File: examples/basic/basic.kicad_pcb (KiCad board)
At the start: 2 copper layers, 9 x 14 mm, 7 parts

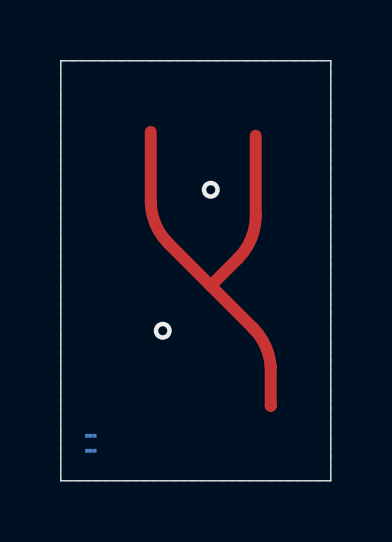
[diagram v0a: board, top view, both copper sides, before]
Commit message: Proof of concept mods for modeling a resistor
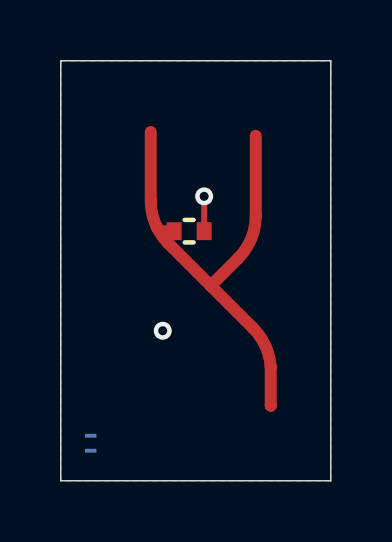
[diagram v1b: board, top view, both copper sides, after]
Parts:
- added R1: 10r 0402 0.1% thinfilm, 1self_passives:R_0402_1005Metric, F.Cu at (144.3, 106.7)
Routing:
- net GND: track 0.00 -> 1.16 mm
- net /MSL: track 16.1 -> 17.2 mm
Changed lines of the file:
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@@
     (property "Sheetfile" "basic.kicad_sch")
     (property "Sheetname" "")
+    (property "ki_description" "Net tie, 2 pins")
+    (property "ki_keywords" "net tie short")
     (attr through_hole exclude_from_pos_files)
     (net_tie_pad_groups "1, 2")
@@
     (at 146.5 103.25 180)
     (descr "Place where port in the simulation should be located. Set it's reference to SPx, where x is port number")
-    (attr board_only exclude_from_pos_files exclude_from_bom)
+    (attr board_only exclude_from_bom)
     (fp_text reference "SP3" (at 0 1 180 unlocked) (layer "F.Fab")
         (effects (font (size 1 1) (thickness 0.15)))
@@
     (at 147 112.75)
     (descr "Place where port in the simulation should be located. Set it's reference to SPx, where x is port number")
-    (attr board_only exclude_from_pos_files exclude_from_bom)
+    (attr board_only exclude_from_bom)
     (fp_text reference "SP2" (at 0 1 unlocked) (layer "F.Fab")
         (effects (font (size 1 1) (thickness 0.15)))
@@
     (property "Sheetfile" "basic.kicad_sch")
     (property "Sheetname" "")
+    (property "ki_description" "Net tie, 2 pins")
+    (property "ki_keywords" "net tie short")
     (attr through_hole exclude_from_pos_files)
     (net_tie_pad_groups "1, 2")
@@
       (net 1 "/MSL") (pinfunction "2") (pintype "passive"))
   )
+  (footprint "1self_passives:R_0402_1005Metric" (layer "F.Cu")
+    (at 144.28 106.68)
+    (descr "Resistor SMD 0402 (1005 Metric), square (rectangular) end terminal, IPC_7351 nominal, (Body size source: http://www.tortai-tech.com/upload/download/2011102023233369053.pdf), generated with kicad-footprint-generator")
+    (tags "resistor")
+    (property "AVR" "TE Connectivity Passive Product")
+    (property "Description" "RES SMD 10 OHM 0.1% 1/16W 0402 ")
+    (property "Detailed Description" "10 Ohms ±0.1% 0.063W, 1/16W Chip Resistor 0402 (1005 Metric)  Thin Film")
+    (property "Mfg Part #" "CPF0402B10RE1")
+    (property "Sheetfile" "basic.kicad_sch")
+    (property "Sheetname" "")
+    (property "similar_resistors" " ")
+    (property "size(LWT,mm)" "1x0.5x0.35")
+    (attr smd)
+    (fp_text reference "R1" (at 0 -1.17) (layer "F.SilkS") hide
+        (effects (font (size 1 1) (thickness 0.15)))
+    )
+    (fp_text value "10r 0402 0.1% thinfilm" (at 0 1.17) (layer "F.Fab") hide
+        (effects (font (size 1 1) (thickness 0.15)))
+    )
+    (fp_text user "${REFERENCE}" (at 0 0) (layer "F.Fab")
+        (effects (font (size 0.25 0.25) (thickness 0.04)))
+    )
+    (fp_line (start -0.15 -0.375) (end 0.15 -0.375)
+      (stroke (width 0.15) (type solid)) (layer "F.SilkS"))
+    (fp_line (start -0.15 0.375) (end 0.15 0.375)
+      (stroke (width 0.15) (type solid)) (layer "F.SilkS"))
+    (fp_line (start -0.7 -0.25) (end -0.7 0.25)
+      (stroke (width 0.05) (type solid)) (layer "F.CrtYd"))
+    (fp_line (start -0.5 0.45) (end 0.5 0.45)
+      (stroke (width 0.05) (type solid)) (layer "F.CrtYd"))
+    (fp_line (start 0.5 -0.45) (end -0.5 -0.45)
+      (stroke (width 0.05) (type solid)) (layer "F.CrtYd"))
+    (fp_line (start 0.7 0.25) (end 0.7 -0.25)
+      (stroke (width 0.05) (type solid)) (layer "F.CrtYd"))
+    (fp_arc (start -0.7 -0.25) (mid -0.641421 -0.391421) (end -0.5 -0.45)
+      (stroke (width 0.05) (type solid)) (layer "F.CrtYd"))
+    (fp_arc (start -0.50187 0.45) (mid -0.643291 0.391421) (end -0.70187 0.25)
+      (stroke (width 0.05) (type solid)) (layer "F.CrtYd"))
+    (fp_arc (start 0.5 -0.45) (mid 0.641421 -0.391421) (end 0.7 -0.25)
+      (stroke (width 0.05) (type solid)) (layer "F.CrtYd"))
+    (fp_arc (start 0.7 0.25) (mid 0.641421 0.391421) (end 0.5 0.45)
+      (stroke (width 0.05) (type solid)) (layer "F.CrtYd"))
+    (fp_line (start -0.5 -0.25) (end 0.5 -0.25)
+      (stroke (width 0.1) (type solid)) (layer "F.Fab"))
+    (fp_line (start -0.5 0.25) (end -0.5 -0.25)
+      (stroke (width 0.1) (type solid)) (layer "F.Fab"))
+    (fp_line (start 0.5 -0.25) (end 0.5 0.25)
+      (stroke (width 0.1) (type solid)) (layer "F.Fab"))
+    (fp_line (start 0.5 0.25) (end -0.5 0.25)
+      (stroke (width 0.1) (type solid)) (layer "F.Fab"))
+    (pad "1" smd rect (at -0.5 0) (size 0.5 0.6) (layers "F.Cu" "F.Paste" "F.Mask")
+      (net 1 "/MSL") (pintype "passive"))
+    (pad "2" smd rect (at 0.5 0) (size 0.5 0.6) (layers "F.Cu" "F.Paste" "F.Mask")
+      (net 2 "GND") (pintype "passive"))
+    (model "${KICAD6_3DMODEL_DIR}/Resistor_SMD.3dshapes/R_0402_1005Metric.wrl"
+      (offset (xyz 0 0 0))
+      (scale (xyz 1 1 1))
+      (rotate (xyz 0 0 0))
+    )
+  )
   (footprint "antmicro-footprints:Simulation_Port" (layer "F.Cu")
     (at 143 103.25 180)
     (descr "Place where port in the simulation should be located. Set it's reference to SPx, where x is port number")
-    (attr board_only exclude_from_pos_files exclude_from_bom)
+    (attr board_only exclude_from_bom)
     (fp_text reference "SP1" (at 0 1 180 unlocked) (layer "F.Fab")
         (effects (font (size 1 1) (thickness 0.15)))
@@
     (property "Sheetfile" "basic.kicad_sch")
     (property "Sheetname" "")
+    (property "ki_description" "Net tie, 2 pins")
+    (property "ki_keywords" "net tie short")
     (attr through_hole exclude_from_pos_files)
     (net_tie_pad_groups "1, 2")
@@
     (property "Sheetfile" "basic.kicad_sch")
     (property "Sheetname" "")
+    (property "ki_description" "Net tie, 2 pins")
+    (property "ki_keywords" "net tie short")
     (attr through_hole exclude_from_pos_files)
     (net_tie_pad_groups "1, 2")
@@
   (segment (start 145 108.5) (end 145.914214 107.585786) (width 0.4) (layer "F.Cu") (net 1))
   (segment (start 146.998156 111.19746) (end 146.998156 112.498156) (width 0.4) (layer "F.Cu") (net 1))
+  (segment (start 143.773792 106.686208) (end 143.78 106.68) (width 0.4) (layer "F.Cu") (net 1))
   (segment (start 146.5 106.171573) (end 146.5 103.5) (width 0.4) (layer "F.Cu") (net 1))
+  (segment (start 143.585787 107.085787) (end 143.585787 106.874213) (width 0.4) (layer "F.Cu") (net 1))
   (segment (start 143 103.373) (end 143 105.671573) (width 0.4) (layer "F.Cu") (net 1))
+  (segment (start 143.323876 106.686208) (end 143.773792 106.686208) (width 0.4) (layer "F.Cu") (net 1))
   (segment (start 146.998156 112.498156) (end 147 112.5) (width 0.4) (layer "F.Cu") (net 1))
   (segment (start 143.585787 107.085787) (end 145 108.5) (width 0.4) (layer "F.Cu") (net 1))
+  (segment (start 143.585787 106.874213) (end 143.78 106.68) (width 0.4) (layer "F.Cu") (net 1))
   (segment (start 145 108.5) (end 146.414214 109.914214) (width 0.4) (layer "F.Cu") (net 1))
+  (segment (start 143.218834 106.581166) (end 143.323876 106.686208) (width 0.4) (layer "F.Cu") (net 1))
   (arc (start 146.414214 109.914214) (mid 146.82172 110.503015) (end 146.998156 111.19746) (width 0.4) (layer "F.Cu") (net 1))
   (arc (start 145.914214 107.585786) (mid 146.34775 106.936938) (end 146.5 106.171573) (width 0.4) (layer "F.Cu") (net 1))
   (arc (start 143 105.671573) (mid 143.15225 106.436939) (end 143.585787 107.085787) (width 0.4) (layer "F.Cu") (net 1))
-  (via (at 145 105.3) (size 0.6) (drill 0.3) (layers "F.Cu" "B.Cu") (free) (net 2))
+  (segment (start 144.78 105.52) (end 144.78 106.68) (width 0.2) (layer "F.Cu") (net 2))
+  (via (at 144.78 105.52) (size 0.6) (drill 0.3) (layers "F.Cu" "B.Cu") (free) (net 2))
   (via (at 143.4 110) (size 0.6) (drill 0.3) (layers "F.Cu" "B.Cu") (free) (net 2))
   (zone (net 2) (net_name "GND") (layer "B.Cu") (hatch edge 0.508)
